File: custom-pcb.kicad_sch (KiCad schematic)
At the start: 26 parts

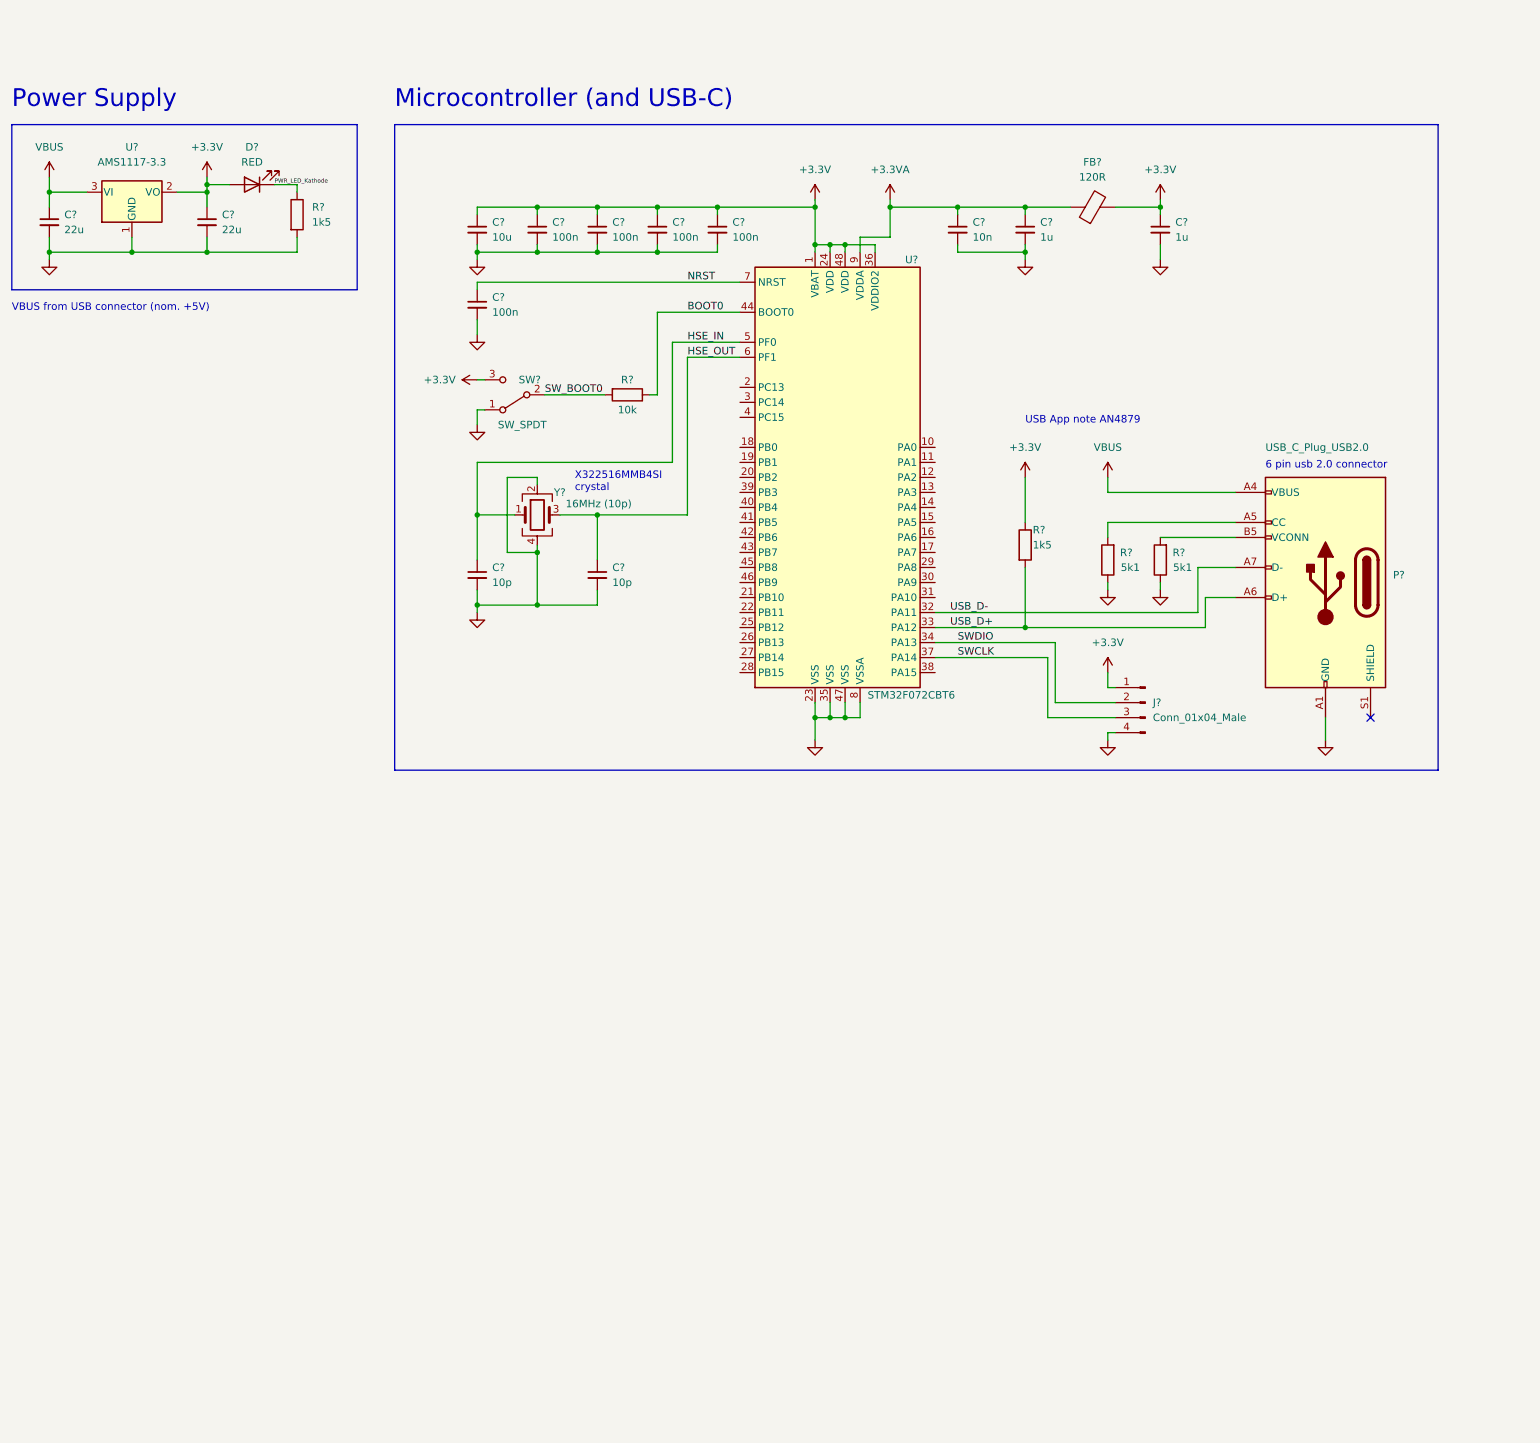
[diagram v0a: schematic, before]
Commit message: Key Switches added
also USB C connector fixed
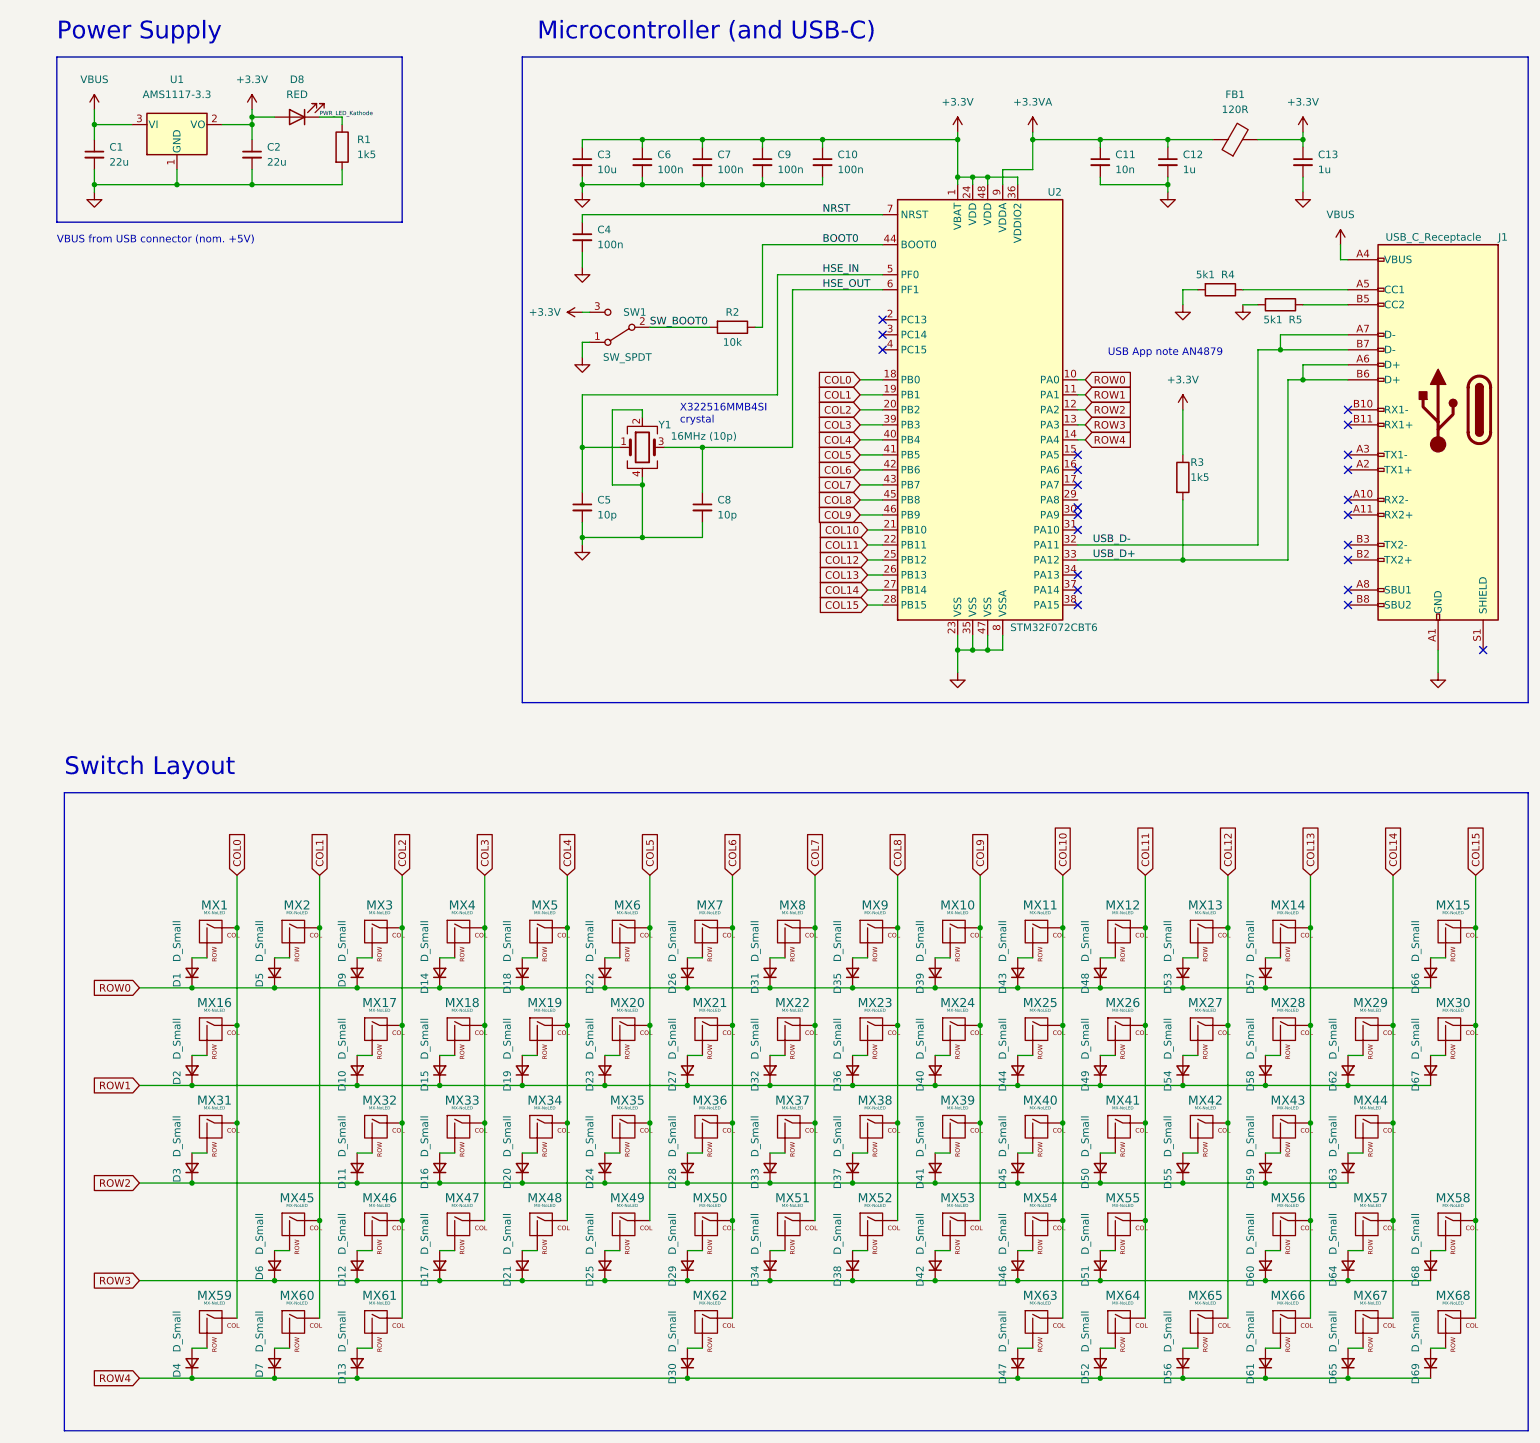
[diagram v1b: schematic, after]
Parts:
- removed J?: Conn_01x04_Male, symbol Connector:Conn_01x04_Male
- removed P?: USB_C_Plug_USB2.0, symbol Connector:USB_C_Plug_USB2.0
- added D1, D10, D11, D12, D13, D14, D15, D16, D17, D18, D19, D2, D20, D21, D22, D23, D24, D25, D26, D27, D28, D29, D3, D30, D31, D32, D33, D34, D35, D36, D37, D38, D39, D4, D40, D41, D42, D43, D44, D45, D46, D47, D48, D49, D5, D50, D51, D52, D53, D54, D55, D56, D57, D58, D59, D6, D60, D61, D62, D63, D64, D65, D66, D67, D68, D69, D7, D9: D_Small, Diode_SMD:D_SOD-123, symbol Device:D_Small
- added J1: USB_C_Receptacle, Connector_USB:USB_C_Receptacle_Amphenol_12401548E4-2A, symbol Connector:USB_C_Receptacle
- added MX1, MX10, MX11, MX12, MX13, MX14, MX15, MX16, MX17, MX18, MX19, MX2, MX20, MX21, MX22, MX23, MX24, MX25, MX26, MX27, MX28, MX29, MX3, MX30, MX31, MX32, MX33, MX34, MX35, MX36, MX37, MX38, MX39, MX4, MX40, MX41, MX42, MX43, MX44, MX45, MX46, MX47, MX48, MX49, MX5, MX50, MX51, MX52, MX53, MX54, MX55, MX56, MX57, MX58, MX59, MX6, MX60, MX61, MX62, MX63, MX64, MX65, MX66, MX67, MX68, MX7, MX8, MX9: MX-NoLED, Button_Switch_Keyboard:SW_Cherry_MX_1.00u_PCB, symbol MX_Alps_Hybrid:MX-NoLED
- C1, C2: renamed from C?; footprint (none) -> Capacitor_SMD:C_0805_2012Metric
- C10, C11, C12, C13, C4, C5, C6, C7, C8, C9: renamed from C?; footprint (none) -> Capacitor_SMD:C_0402_1005Metric
- C3: renamed from C?; footprint (none) -> Capacitor_SMD:C_0603_1608Metric
- D8: renamed from D?; footprint (none) -> LED_SMD:LED_0603_1608Metric
- FB1: renamed from FB?; footprint (none) -> Inductor_SMD:L_0603_1608Metric
- R1, R2, R3, R4, R5: renamed from R?; footprint (none) -> Resistor_SMD:R_0402_1005Metric
- SW1: renamed from SW?; footprint (none) -> Button_Switch_SMD:SW_Push_1P1T-MP_NO_Horizontal_Alps_SKRTLAE010
- Y1: renamed from Y?; footprint (none) -> Crystal:Crystal_SMD_3225-4Pin_3.2x2.5mm
- gave numbers to parts that had none: 2
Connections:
- net GND: now also R4.2, R5.2, J1.A1 (GND), J1.A12 (GND), J1.B1 (GND), J1.B12 (GND); no longer R4.1, R5.1
- net USB_D+: now also J1.A6 (D+), J1.B6 (D+)
- net USB_D-: now also J1.A7 (D-), J1.B7 (D-)
- net VBUS: now also J1.A4 (VBUS), J1.A9 (VBUS), J1.B4 (VBUS), J1.B9 (VBUS)
- net ROW0: now reaches U2.10 (PA0)
- net ROW0: now also D1.1 (K), D14.1 (K), D18.1 (K), D22.1 (K), D26.1 (K), D31.1 (K), D35.1 (K), D39.1 (K), D43.1 (K), D48.1 (K), D5.1 (K), D53.1 (K), D57.1 (K), D66.1 (K), D9.1 (K)
- net ROW1: now reaches U2.11 (PA1)
- net ROW1: now also D10.1 (K), D15.1 (K), D19.1 (K), D2.1 (K), D23.1 (K), D27.1 (K), D32.1 (K), D36.1 (K), D40.1 (K), D44.1 (K), D49.1 (K), D54.1 (K), D58.1 (K), D62.1 (K), D67.1 (K)
- net ROW2: now reaches U2.12 (PA2)
- net ROW2: now also D11.1 (K), D16.1 (K), D20.1 (K), D24.1 (K), D28.1 (K), D3.1 (K), D33.1 (K), D37.1 (K), D41.1 (K), D45.1 (K), D50.1 (K), D55.1 (K), D59.1 (K), D63.1 (K)
- net ROW3: now reaches U2.13 (PA3)
- net ROW3: now also D12.1 (K), D17.1 (K), D21.1 (K), D25.1 (K), D29.1 (K), D34.1 (K), D38.1 (K), D42.1 (K), D46.1 (K), D51.1 (K), D6.1 (K), D60.1 (K), D64.1 (K), D68.1 (K)
- net ROW4: now reaches U2.14 (PA4)
- net ROW4: now also D13.1 (K), D30.1 (K), D4.1 (K), D47.1 (K), D52.1 (K), D56.1 (K), D61.1 (K), D65.1 (K), D69.1 (K), D7.1 (K)
- net COL0: now reaches U2.18 (PB0)
- net COL0: now also MX1.1 (COL), MX16.1 (COL), MX31.1 (COL), MX59.1 (COL)
- net COL1: now reaches U2.19 (PB1)
- net COL1: now also MX2.1 (COL), MX45.1 (COL), MX60.1 (COL)
- net COL2: now reaches U2.20 (PB2)
- net COL2: now also MX17.1 (COL), MX3.1 (COL), MX32.1 (COL), MX46.1 (COL), MX61.1 (COL)
- net COL10: now reaches U2.21 (PB10)
- net COL10: now also MX11.1 (COL), MX25.1 (COL), MX40.1 (COL), MX54.1 (COL), MX63.1 (COL)
- net COL11: now reaches U2.22 (PB11)
- net COL11: now also MX12.1 (COL), MX26.1 (COL), MX41.1 (COL), MX55.1 (COL), MX64.1 (COL)
- net COL12: now reaches U2.25 (PB12)
- net COL12: now also MX13.1 (COL), MX27.1 (COL), MX42.1 (COL), MX65.1 (COL)
- net COL13: now reaches U2.26 (PB13)
- net COL13: now also MX14.1 (COL), MX28.1 (COL), MX43.1 (COL), MX56.1 (COL), MX66.1 (COL)
- net COL14: now reaches U2.27 (PB14)
- net COL14: now also MX29.1 (COL), MX44.1 (COL), MX57.1 (COL), MX67.1 (COL)
- net COL15: now reaches U2.28 (PB15)
- net COL15: now also MX15.1 (COL), MX30.1 (COL), MX58.1 (COL), MX68.1 (COL)
- net COL3: now reaches U2.39 (PB3)
- net COL3: now also MX18.1 (COL), MX33.1 (COL), MX4.1 (COL), MX47.1 (COL)
- net COL4: now reaches U2.40 (PB4)
- net COL4: now also MX19.1 (COL), MX34.1 (COL), MX48.1 (COL), MX5.1 (COL)
- net COL5: now reaches U2.41 (PB5)
- net COL5: now also MX20.1 (COL), MX35.1 (COL), MX49.1 (COL), MX6.1 (COL)
- net COL6: now reaches U2.42 (PB6)
- net COL6: now also MX21.1 (COL), MX36.1 (COL), MX50.1 (COL), MX62.1 (COL), MX7.1 (COL)
- net COL7: now reaches U2.43 (PB7)
- net COL7: now also MX22.1 (COL), MX37.1 (COL), MX51.1 (COL), MX8.1 (COL)
- net COL8: now reaches U2.45 (PB8)
- net COL8: now also MX23.1 (COL), MX38.1 (COL), MX52.1 (COL), MX9.1 (COL)
- net COL9: now reaches U2.46 (PB9)
- net COL9: now also MX10.1 (COL), MX24.1 (COL), MX39.1 (COL), MX53.1 (COL)
- net SWCLK: no longer names the net of U2.37 (PA14)
- net SWDIO: no longer names the net of U2.34 (PA13)
- new net: D18.2 (A), MX5.2 (ROW)
- new net: D11.2 (A), MX32.2 (ROW)
- new net: D7.2 (A), MX60.2 (ROW)
- new net: D23.2 (A), MX20.2 (ROW)
- new net: D63.2 (A), MX44.2 (ROW)
- new net: D61.2 (A), MX66.2 (ROW)
- new net: D16.2 (A), MX33.2 (ROW)
- new net: D41.2 (A), MX39.2 (ROW)
- new net: D57.2 (A), MX14.2 (ROW)
- new net: D3.2 (A), MX31.2 (ROW)
- new net: D47.2 (A), MX63.2 (ROW)
- new net: D48.2 (A), MX12.2 (ROW)
- new net: D2.2 (A), MX16.2 (ROW)
- new net: D69.2 (A), MX68.2 (ROW)
- new net: J1.B5 (CC2), R5.1
- new net: D37.2 (A), MX38.2 (ROW)
- new net: D54.2 (A), MX27.2 (ROW)
- new net: D21.2 (A), MX48.2 (ROW)
- new net: D46.2 (A), MX54.2 (ROW)
- new net: D62.2 (A), MX29.2 (ROW)
- new net: D32.2 (A), MX22.2 (ROW)
- new net: D60.2 (A), MX56.2 (ROW)
- new net: D14.2 (A), MX4.2 (ROW)
- new net: D39.2 (A), MX10.2 (ROW)
- new net: D30.2 (A), MX62.2 (ROW)
- new net: D55.2 (A), MX42.2 (ROW)
- new net: D38.2 (A), MX52.2 (ROW)
- new net: D31.2 (A), MX8.2 (ROW)
- new net: D24.2 (A), MX35.2 (ROW)
- new net: D17.2 (A), MX47.2 (ROW)
- new net: D51.2 (A), MX55.2 (ROW)
- new net: D49.2 (A), MX26.2 (ROW)
- new net: D44.2 (A), MX25.2 (ROW)
- new net: D56.2 (A), MX65.2 (ROW)
- new net: D19.2 (A), MX19.2 (ROW)
- new net: D43.2 (A), MX11.2 (ROW)
- new net: D12.2 (A), MX46.2 (ROW)
- new net: D42.2 (A), MX53.2 (ROW)
- new net: D36.2 (A), MX23.2 (ROW)
- new net: D4.2 (A), MX59.2 (ROW)
- new net: D34.2 (A), MX51.2 (ROW)
- new net: D45.2 (A), MX40.2 (ROW)
- new net: D6.2 (A), MX45.2 (ROW)
- new net: D58.2 (A), MX28.2 (ROW)
- new net: D64.2 (A), MX57.2 (ROW)
- new net: D68.2 (A), MX58.2 (ROW)
- new net: D13.2 (A), MX61.2 (ROW)
- new net: D1.2 (A), MX1.2 (ROW)
- new net: D5.2 (A), MX2.2 (ROW)
- new net: D9.2 (A), MX3.2 (ROW)
- new net: D27.2 (A), MX21.2 (ROW)
- new net: D28.2 (A), MX36.2 (ROW)
- new net: D20.2 (A), MX34.2 (ROW)
- new net: D66.2 (A), MX15.2 (ROW)
- new net: D35.2 (A), MX9.2 (ROW)
- new net: D52.2 (A), MX64.2 (ROW)
- new net: D10.2 (A), MX17.2 (ROW)
- new net: D15.2 (A), MX18.2 (ROW)
- new net: D33.2 (A), MX37.2 (ROW)
- new net: D22.2 (A), MX6.2 (ROW)
- new net: D25.2 (A), MX49.2 (ROW)
- new net: D40.2 (A), MX24.2 (ROW)
- new net: D53.2 (A), MX13.2 (ROW)
- new net: D26.2 (A), MX7.2 (ROW)
- new net: D50.2 (A), MX41.2 (ROW)
- new net: D65.2 (A), MX67.2 (ROW)
- new net: D29.2 (A), MX50.2 (ROW)
- new net: D59.2 (A), MX43.2 (ROW)
- new net: J1.A5 (CC1), R4.1
- new net: D67.2 (A), MX30.2 (ROW)
- no-connect marks 1 -> 23
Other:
- note added: "Switch Layout"
- note removed: "6 pin usb 2.0 connector"
- moved on the sheet: C1, C10, C11, C12, C13, C2, C3, C4, C5, C6, C7, C8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

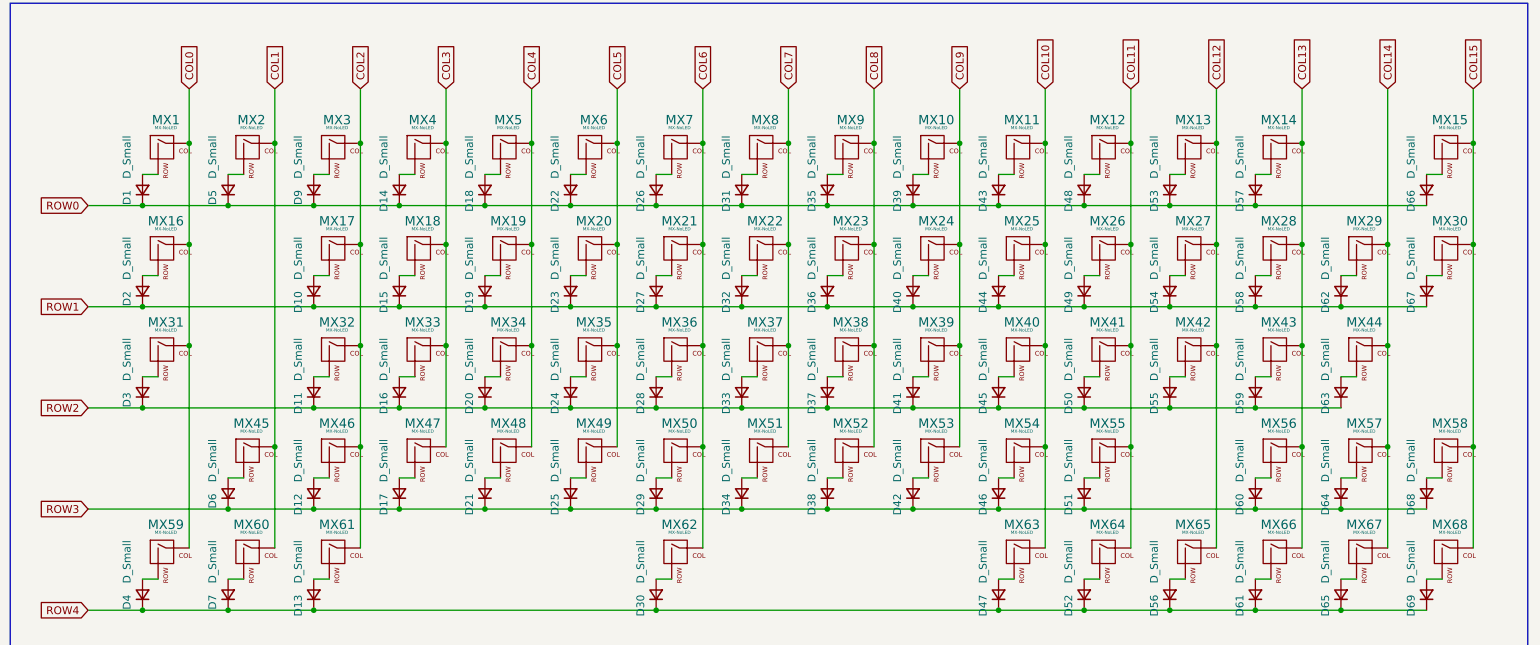
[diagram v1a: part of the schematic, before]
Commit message: Footprints added
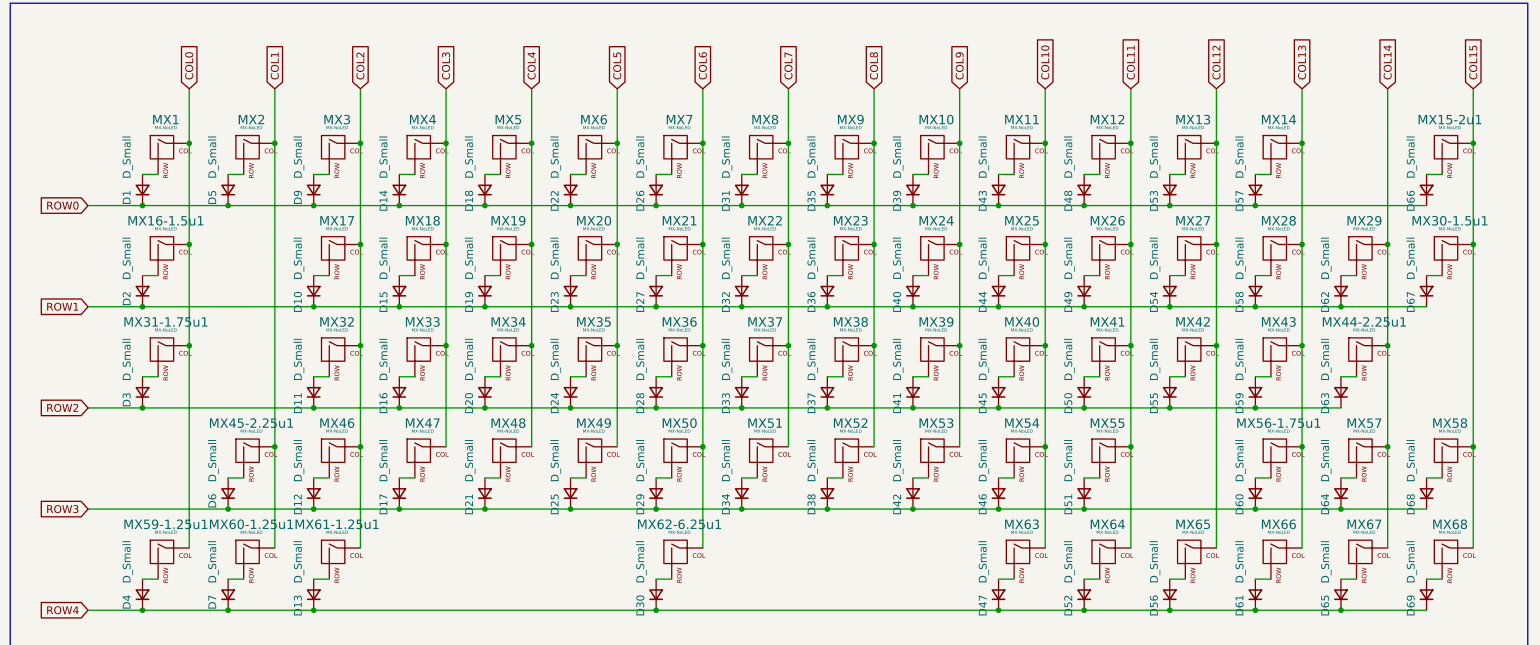
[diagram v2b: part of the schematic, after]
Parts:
- MX1, MX10, MX11, MX12, MX13, MX14, MX17, MX18, MX19, MX2, MX20, MX21, MX22, MX23, MX24, MX25, MX26, MX27, MX28, MX29, MX3, MX32, MX33, MX34, MX35, MX36, MX37, MX38, MX39, MX4, MX40, MX41, MX42, MX43, MX46, MX47, MX48, MX49, MX5, MX50, MX51, MX52, MX53, MX54, MX55, MX57, MX58, MX6, MX63, MX64, MX65, MX66, MX67, MX68, MX7, MX8, MX9: footprint Button_Switch_Keyboard:SW_Cherry_MX_1.00u_PCB -> MX_Alps_Hybrid:MX-1U-NoLED
- MX15-2u1: renamed from MX15; footprint Button_Switch_Keyboard:SW_Cherry_MX_1.00u_PCB -> MX_Alps_Hybrid:MX-2U-NoLED
- MX16-1.5u1: renamed from MX16; footprint Button_Switch_Keyboard:SW_Cherry_MX_1.00u_PCB -> MX_Alps_Hybrid:MX-1.5U-NoLED
- MX30-1.5u1: renamed from MX30; footprint Button_Switch_Keyboard:SW_Cherry_MX_1.00u_PCB -> MX_Alps_Hybrid:MX-1.5U-NoLED
- MX31-1.75u1: renamed from MX31; footprint Button_Switch_Keyboard:SW_Cherry_MX_1.00u_PCB -> MX_Alps_Hybrid:MX-1.75U-NoLED
- MX44-2.25u1: renamed from MX44; footprint Button_Switch_Keyboard:SW_Cherry_MX_1.00u_PCB -> MX_Alps_Hybrid:MX-2.25U-NoLED
- MX45-2.25u1: renamed from MX45; footprint Button_Switch_Keyboard:SW_Cherry_MX_1.00u_PCB -> MX_Alps_Hybrid:MX-2.25U-NoLED
- MX56-1.75u1: renamed from MX56; footprint Button_Switch_Keyboard:SW_Cherry_MX_1.00u_PCB -> MX_Alps_Hybrid:MX-1.75U-NoLED
- MX59-1.25u1: renamed from MX59; footprint Button_Switch_Keyboard:SW_Cherry_MX_1.00u_PCB -> MX_Alps_Hybrid:MX-1.25U-NoLED
- MX60-1.25u1: renamed from MX60; footprint Button_Switch_Keyboard:SW_Cherry_MX_1.00u_PCB -> MX_Alps_Hybrid:MX-1.25U-NoLED
- MX61-1.25u1: renamed from MX61; footprint Button_Switch_Keyboard:SW_Cherry_MX_1.00u_PCB -> MX_Alps_Hybrid:MX-1.25U-NoLED
- MX62-6.25u1: renamed from MX62; footprint Button_Switch_Keyboard:SW_Cherry_MX_1.00u_PCB -> MX_Alps_Hybrid:MX-6.25U-ReversedStabilizers-NoLED
